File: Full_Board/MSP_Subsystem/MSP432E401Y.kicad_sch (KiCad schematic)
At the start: 4 parts, among them J1-J3 Conn_01x10, J4-J2 Conn_01x10, J5-J7 Conn_01x10, J8-J6 Conn_01x10

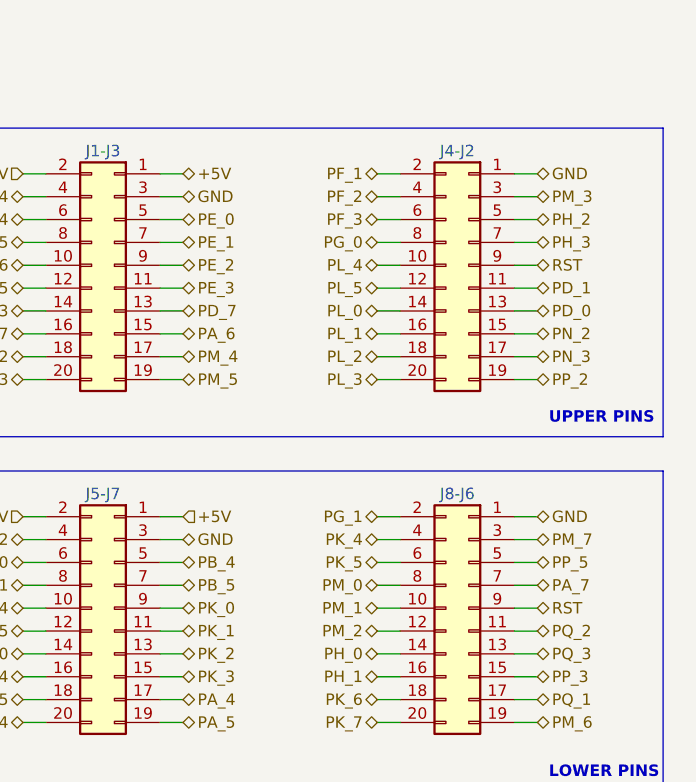
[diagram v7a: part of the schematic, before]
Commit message: Corrections to the power supply
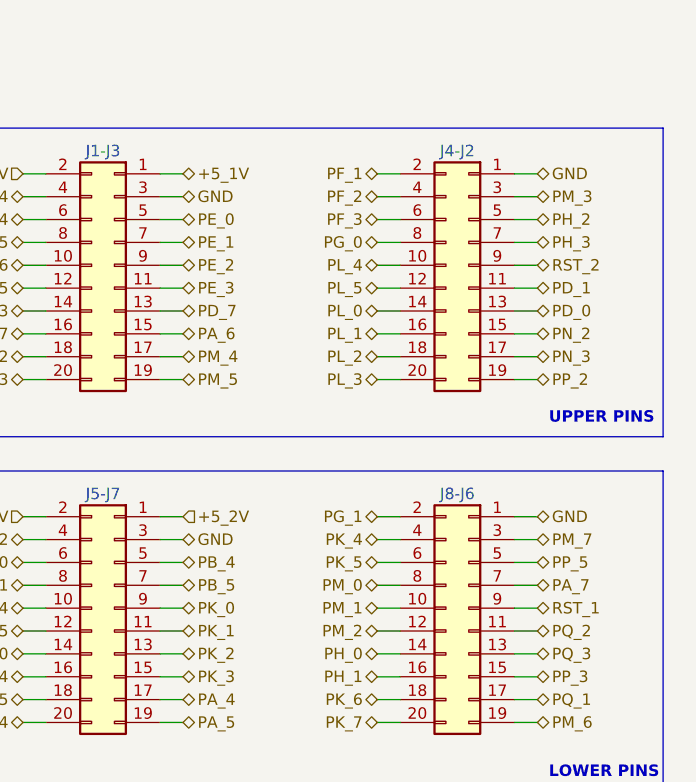
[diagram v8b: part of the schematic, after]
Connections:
- net +5V renamed +5_1V
- net +5_1V: no longer J5-J7.1 (Pin_1)
- net RST renamed RST_1
- net RST_1: no longer J4-J2.9 (Pin_9)
- new net +5_2V: J5-J7.1 (Pin_1)
- new net RST_2: J4-J2.9 (Pin_9)
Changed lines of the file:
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@@
     (effects (font (size 1.27 1.27) bold) (justify left bottom))
   )
-  (hierarchical_label "RST" (shape bidirectional) (at 177.8 71.12 0)
+  (hierarchical_label "RST_2" (shape bidirectional) (at 177.8 71.12 0)
     (effects (font (size 1.27 1.27)) (justify left))
   )
@@
     (effects (font (size 1.27 1.27)) (justify left))
   )
-  (hierarchical_label "+5V" (shape input) (at 138.43 99.06 0)
+  (hierarchical_label "+5_2V" (shape input) (at 138.43 99.06 0)
     (effects (font (size 1.27 1.27)) (justify left))
   )
@@
     (effects (font (size 1.27 1.27)) (justify left))
   )
-  (hierarchical_label "RST" (shape bidirectional) (at 177.8 109.22 0)
+  (hierarchical_label "RST_1" (shape bidirectional) (at 177.8 109.22 0)
     (effects (font (size 1.27 1.27)) (justify left))
   )
@@
     (effects (font (size 1.27 1.27)) (justify left))
   )
-  (hierarchical_label "+5V" (shape bidirectional) (at 138.43 60.96 0)
-    (effects (font (size 1.27 1.27)) (justify left))
-  )
+  (hierarchical_label "+5_1V" (shape bidirectional) (at 138.43 60.96 0)
+    (effects (font (size 1.27 1.27)) (justify left))
+  )
